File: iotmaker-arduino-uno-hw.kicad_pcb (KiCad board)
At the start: 2 copper layers, 68.5 x 53.3 mm, 53 parts, among them J1 BARREL_JACK, J2 USB_A, J3 header Analog, J4 Header I2C, J5 Header module, J6 CONN_02X03, Q1 SI2301DS_GSD, SW1 RESET, SW2 SW_PUSH, U1 CH340G, U2 ATMEGA328P-AU, U3 LM358, U4 FAN1117A-3.3v, U5 FAN1117A-5.0v, Y1 16MHz_GND24, Y2 12MHz_GND24

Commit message: basic completed pcb
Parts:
- added G***: LOGO, footprint:label-arduino-pwr, F.Cu at (172.4, 79.9)
- added G***: LOGO, footprint:logo_openhardware_5x5mm, F.Cu at (176.5, 73.2)
- added G***: LOGO, footprint:logo-iotmaker-v1, F.Cu at (182.4, 68.2)
- added G***: LOGO, footprint:label-arduino-pin3, F.Cu at (172.4, 85.5)
- added G***: LOGO, footprint:label-arduino-pin8, F.Cu at (150.6, 67.0)
- added G***: LOGO, footprint:label-arduino-rst, F.Cu at (143.8, 67.0)
- added G***: LOGO, footprint:label-arduino-uno, F.Cu at (189.8, 68.2)
- added G***: LOGO, footprint:label-arduino-power, F.Cu at (182.5, 103.1)
- added G***: LOGO, footprint:label-arduino-analog, F.Cu at (195.1, 103.0)
- added G***: LOGO, footprint:label-arduino-digital, F.Cu at (174.0, 66.6)
- added G***: LOGO, footprint:logo_cc-bby-sa_14.1x5mm, F.Cu at (186.9, 73.2)
- added J7: Header Analog, Pin_Headers:Pin_Header_Straight_1x05_Pitch2.54mm, F.Cu at (201.5, 77.1)
- added J8: DHT, Pin_Headers:Pin_Header_Straight_1x03_Pitch2.54mm, F.Cu at (205.4, 92.7)
- J3: value header Analog -> Servo
- moved J5 26.3 mm to (201.5, 92.7)
- moved R9 13.3 mm to (170.2, 79.1), turned to 180 degrees
- moved D5 10.2 mm to (170.2, 80.8), turned to 0 degrees
- moved J4 9.54 mm to (198.1, 92.7)
- moved Q1 6.35 mm to (168.1, 91.4), turned to 270 degrees
- moved R10 6.03 mm to (170.2, 86.2)
- moved R4 5.47 mm to (168.1, 103.5)
- moved R3 4.87 mm to (173.4, 98.3), turned to 90 degrees
- moved U3 4.18 mm to (169.4, 98.3)
- moved D4 3.88 mm to (170.2, 73.1), turned to 0 degrees
- moved C5 3.61 mm to (184.5, 99.1), turned to 0 degrees
- moved R2 2.84 mm to (175.1, 98.3), turned to 270 degrees
- moved C11 2.54 mm to (159.5, 67.7)
- moved D2 2.50 mm to (171.4, 103.5), turned to 180 degrees
- moved R5 2.48 mm to (171.1, 69.3), turned to 90 degrees
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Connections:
- J3 pad 3: ADC6 -> PB1
- J5 pad 3: PD2 -> PD4
- J5 pad 4: ADC7 -> ADC6
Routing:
- net GND: track 12.8 -> 361.1 mm, vias 0 -> 17
- net +5V: track 13.0 -> 226.3 mm, vias 0 -> 8
- net PC6/RESET: track 6.14 -> 174.5 mm, vias 0 -> 3
- net +3V3: track 0.00 -> 108.7 mm, vias 0 -> 1
- net PC4: track 24.8 -> 126.7 mm, vias 0 -> 2
- net PC5: track 27.1 -> 125.1 mm, vias 0 -> 2
- net AREF: track 3.21 -> 64.7 mm
- net PB5: track 47.5 -> 103.4 mm, vias 0 -> 3
- net PD1/TXD: track 31.9 -> 85.5 mm, vias 0 -> 2
- net Net-(J2-Pad1): track 0.00 -> 52.7 mm, vias 0 -> 2
- net PD0/RXD: track 33.9 -> 84.4 mm, vias 0 -> 2
- net PB0: track 36.8 -> 85.6 mm, vias 0 -> 1
- net ADC7: track 0.00 -> 47.3 mm, vias 0 -> 2
- net PD4: track 28.5 -> 67.9 mm, vias 0 -> 1
- net VCC: track 0.00 -> 38.5 mm
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- added copper zone on B.Cu, net GND
- added copper zone on F.Cu, net GND
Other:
- net class Default: clearance 0.3 -> 0.1; via_dia 0.8 -> 1; via_drill 0.4 -> 0.5
- net class VCC added: clearance 0.3, trace_width 1.5, via_dia 1.2, via_drill 0.7
- rule trace_clearance: 0.3 -> 0.1
- board text added: "0"
- board text added: "1"
- board text added: "10"
- board text added: "11"
- board text added: "12"
- board text added: "13"
- board text added: "2"
- board text added: "3"
- board text added: "3.3V"
- board text added: "4"
- board text added: "5"
- board text added: "5V"
- board text added: "6"
- board text added: "7"
- board text added: "8"
- board text added: "9"
- board text added: "A0"
- board text added: "A1"
- board text added: "A2"
- board text added: "A3"
- board text added: "A4"
- board text added: "A5"
- board text added: "A6"
- board text added: "A7"
- board text added: "AREF"
- board text added: "GND"
- board text added: "ICSP"
- board text added: "IOREF"
- board text added: "RST"
- board text added: "RX"
- board text added: "SCL"
- board text added: "SCL/A5"
- board text added: "SDA"
- board text added: "SDA/A4"
- board text added: "TX"
- board text added: "Vin"
- board text added: "https://iotmaker.vn"
- board text added: "~~"
- board text added: "~~9"

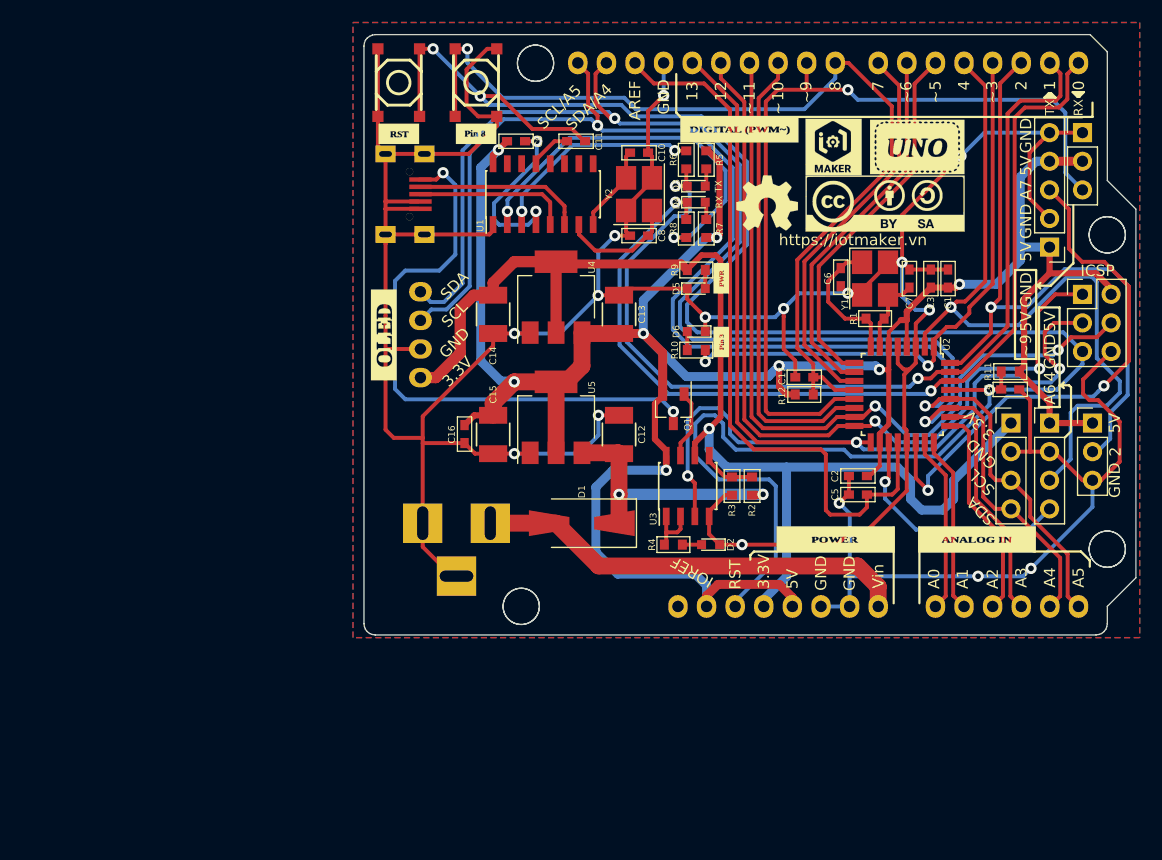
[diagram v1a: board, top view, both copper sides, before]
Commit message: cchange CH340G to CH340E & update information board, gerber file
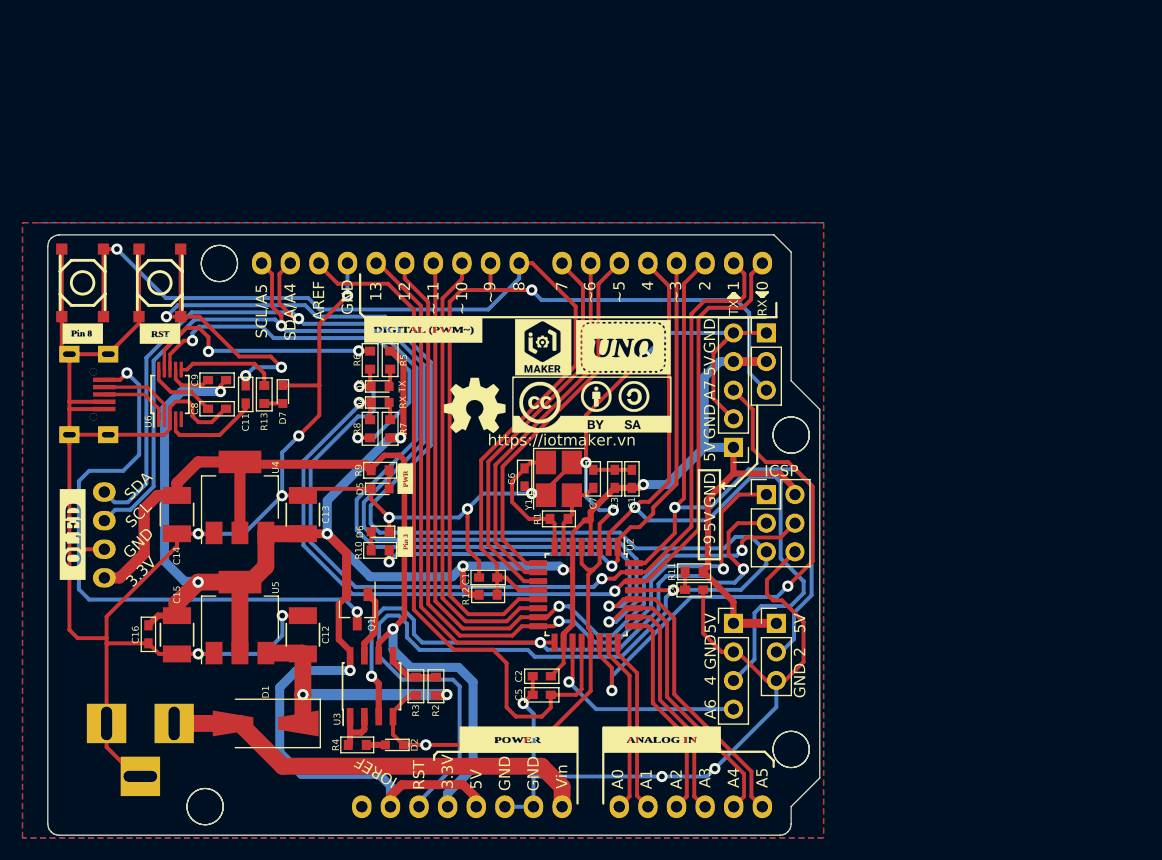
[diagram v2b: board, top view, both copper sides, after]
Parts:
- removed C10: 22pF, footprint:C_0603
- removed J4: Header I2C, Pin_Headers:Pin_Header_Straight_1x04_Pitch2.54mm
- removed U1: CH340G, Housings_SOIC:SOIC-16_3.9x9.9mm_Pitch1.27mm
- removed Y2: 12MHz_GND24, Crystals:Crystal_SMD_3225-4pin_3.2x2.5mm_HandSoldering
- added D7: LED, LEDs:LED_0603, F.Cu at (133.5, 90.2)
- added R13: 1k, footprint:R_0603, F.Cu at (131.8, 90.2)
- added U6: CH340E, Housings_SSOP:MSOP-10_3x3mm_Pitch0.5mm, F.Cu at (123.5, 90.2)
- C8: value 22pF -> 100nF
- moved C8 40.5 mm to (127.6, 91.4), turned to 180 degrees
- moved SW2 39.2 mm to (115.7, 80.3), turned to 270 degrees
- moved G*** 39.2 mm to (115.7, 84.8)
- moved C11 37.0 mm to (130.2, 90.2), turned to 270 degrees
- moved C9 34.0 mm to (127.6, 88.9), turned to 0 degrees
- moved G*** 33.3 mm to (154.4, 120.8)
- moved C1 33.2 mm to (164.5, 97.7)
- moved C12 33.2 mm to (135.3, 111.5)
- moved C3 33.2 mm to (162.9, 97.7)
- moved C4 33.2 mm to (170.0, 107.5)
- moved C5 33.2 mm to (156.5, 116.8)
- moved C6 33.2 mm to (154.9, 97.5)
- moved C7 33.2 mm to (161.0, 97.7)
- moved D1 33.2 mm to (132.0, 119.4)
- moved D3 33.2 mm to (142.1, 89.5)
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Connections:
- C11 pad 1: Net-(C11-Pad1) -> PC6/RESET
- C11 pad 2: PC6/RESET -> Net-(C11-Pad2)
- C8 pad 2: Net-(C8-Pad2) -> V3
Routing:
- net +3V3: track 108.7 -> 81.7 mm
- net Net-(C9-Pad1): track 15.4 -> 4.14 mm, vias 2 -> 0
- net Net-(C8-Pad2): track 10.5 -> 0.00 mm
- net Net-(R13-Pad2): track 0.00 -> 9.01 mm
- net Net-(C11-Pad2): track 0.00 -> 8.87 mm
- net Net-(J2-Pad2): track 15.3 -> 7.29 mm
- net Net-(C10-Pad2): track 7.73 -> 0.00 mm
- net Net-(J2-Pad3): track 14.0 -> 6.29 mm
- net V3: track 0.00 -> 6.35 mm
- net Net-(C11-Pad1): track 3.80 -> 0.00 mm
- net Net-(R6-Pad1): track 19.3 -> 22.5 mm
- net PB0: track 85.6 -> 88.0 mm
- net ADC6: track 21.6 -> 19.2 mm
- net +5V: track 226.3 -> 224.4 mm
- net Net-(D7-Pad2): track 0.00 -> 1.65 mm
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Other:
- outline, holes or cut-outs redrawn
